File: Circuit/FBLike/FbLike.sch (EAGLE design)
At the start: 6 parts, among them IC1 MAX7219CNG

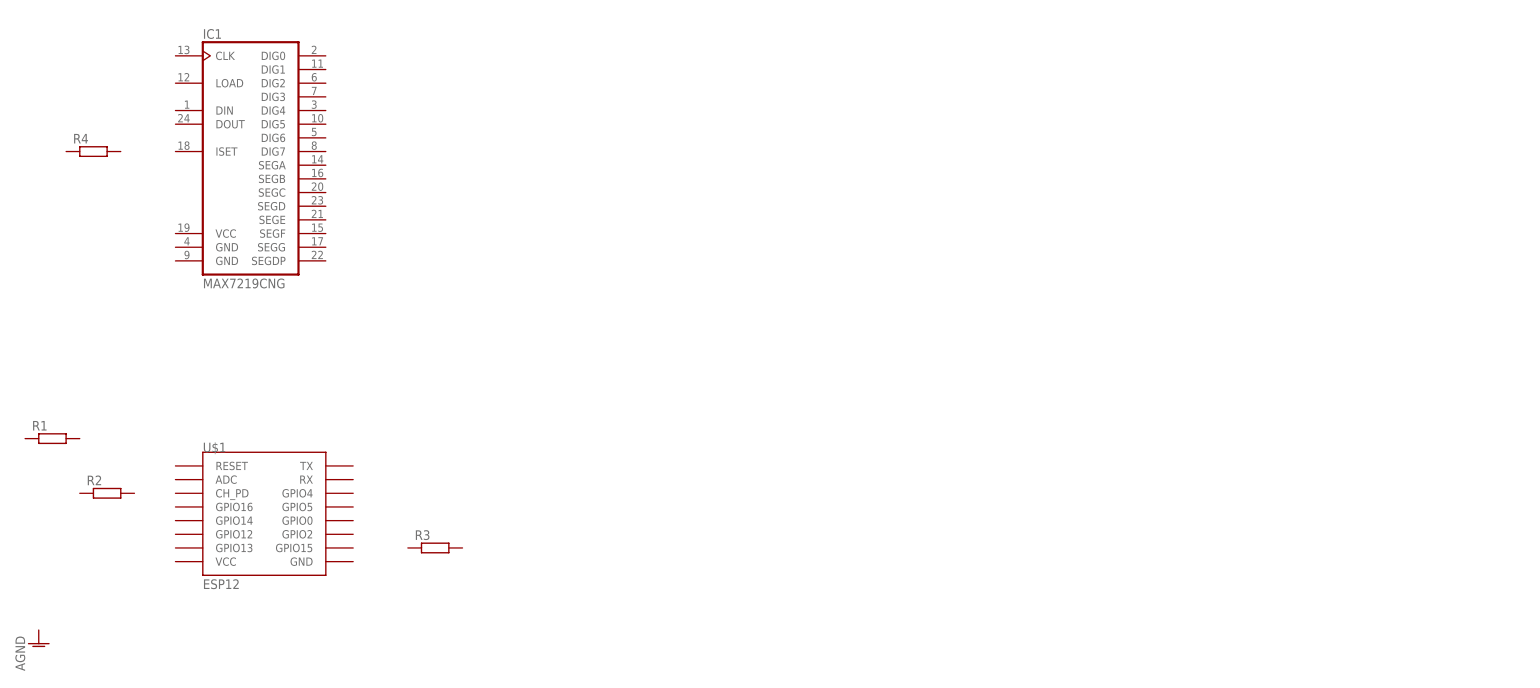
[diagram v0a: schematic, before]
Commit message: Add New Project Use new wifi modular MT7681
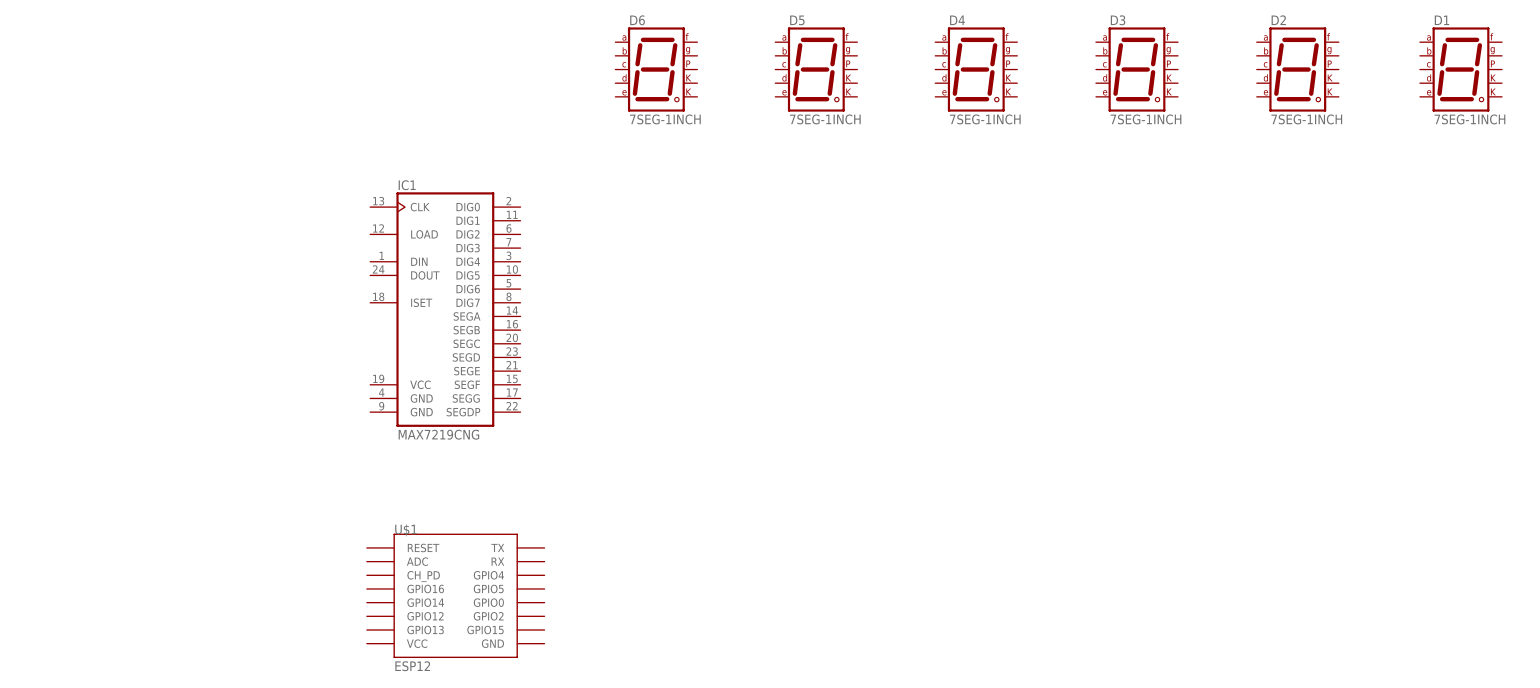
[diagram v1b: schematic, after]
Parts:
- removed R1, R2, R3, R4: (no value), eagle-ltspice:R
- added D1, D2, D3, D4, D5, D6: 7SEG-1INCH, My7Segment:7SEG-1INCH
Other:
- moved on the sheet: IC1, U$1
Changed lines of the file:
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@@
 <part name="IC1" library="maxim" deviceset="MAX7219CNG" device=""/>
 <part name="U$1" library="esp8266modules" deviceset="ESP12" device=""/>
-<part name="R1" library="eagle-ltspice" deviceset="R" device=""/>
-<part name="R2" library="eagle-ltspice" deviceset="R" device=""/>
-<part name="R3" library="eagle-ltspice" deviceset="R" device=""/>
-<part name="R4" library="eagle-ltspice" deviceset="R" device=""/>
-<part name="AGND1" library="supply1" deviceset="AGND" device=""/>
+<part name="D6" library="My7Segment" deviceset="7SEG-1INCH" device=""/>
+<part name="D5" library="My7Segment" deviceset="7SEG-1INCH" device=""/>
+<part name="D4" library="My7Segment" deviceset="7SEG-1INCH" device=""/>
+<part name="D3" library="My7Segment" deviceset="7SEG-1INCH" device=""/>
+<part name="D2" library="My7Segment" deviceset="7SEG-1INCH" device=""/>
+<part name="D1" library="My7Segment" deviceset="7SEG-1INCH" device=""/>
 </parts>
 <sheets>
@@
 </plain>
 <instances>
-<instance part="IC1" gate="G$1" x="-104.14" y="50.8"/>
-<instance part="U$1" gate="G$1" x="-101.6" y="-15.24"/>
-<instance part="R1" gate="G$1" x="-142.24" y="-2.54"/>
-<instance part="R2" gate="G$1" x="-132.08" y="-12.7"/>
-<instance part="R3" gate="G$1" x="-71.12" y="-22.86"/>
-<instance part="R4" gate="G$1" x="-134.62" y="50.8"/>
-<instance part="AGND1" gate="VR1" x="-144.78" y="-40.64"/>
+<instance part="IC1" gate="G$1" x="-67.96" y="22.7"/>
+<instance part="U$1" gate="G$1" x="-66.04" y="-30.48"/>
+<instance part="D6" gate="G$1" x="-30.02" y="66.04"/>
+<instance part="D5" gate="G$1" x="-0.3" y="66.04"/>
+<instance part="D4" gate="G$1" x="29.42" y="66.04"/>
+<instance part="D3" gate="G$1" x="59.28" y="66.04"/>
+<instance part="D2" gate="G$1" x="89.16" y="66.04"/>
+<instance part="D1" gate="G$1" x="119.48" y="66.04"/>
 </instances>
 <busses>
